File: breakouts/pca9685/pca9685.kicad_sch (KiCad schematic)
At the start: 4 parts, among them J1 Conn_01x03, U1 PCA9685PW

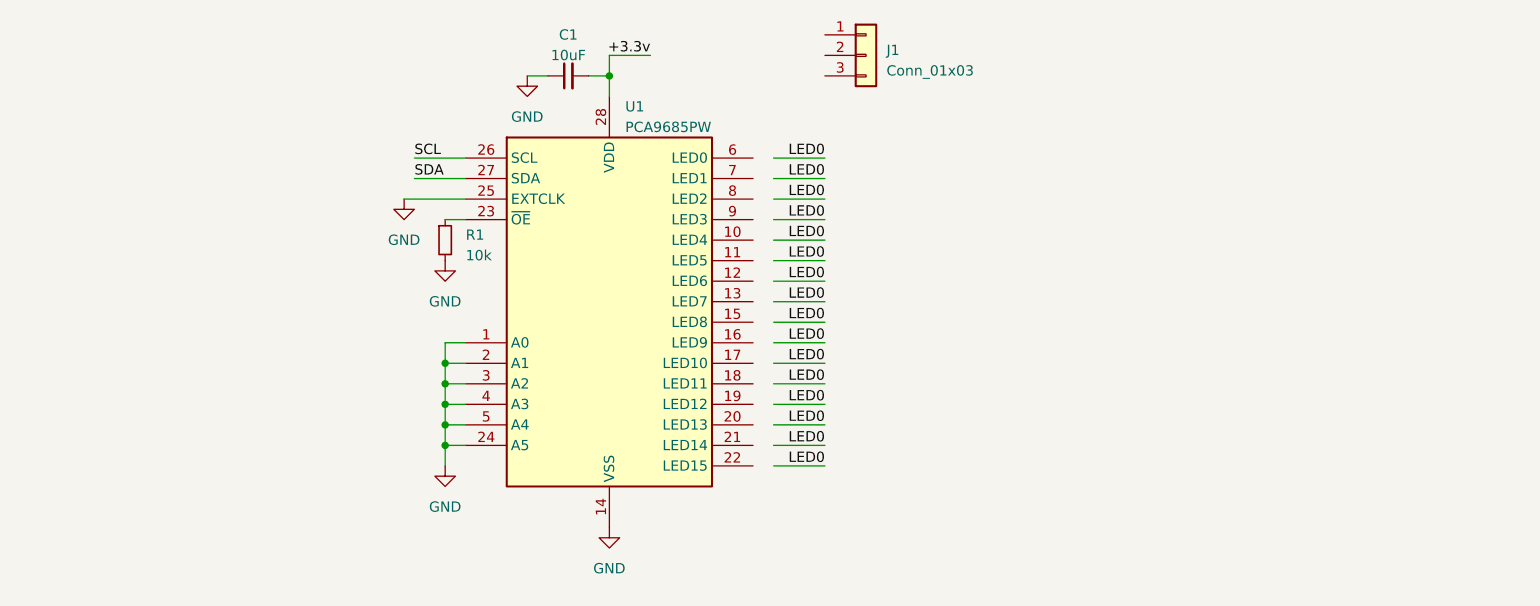
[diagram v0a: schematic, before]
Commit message: Feat[pca9585 breakout]: design complete
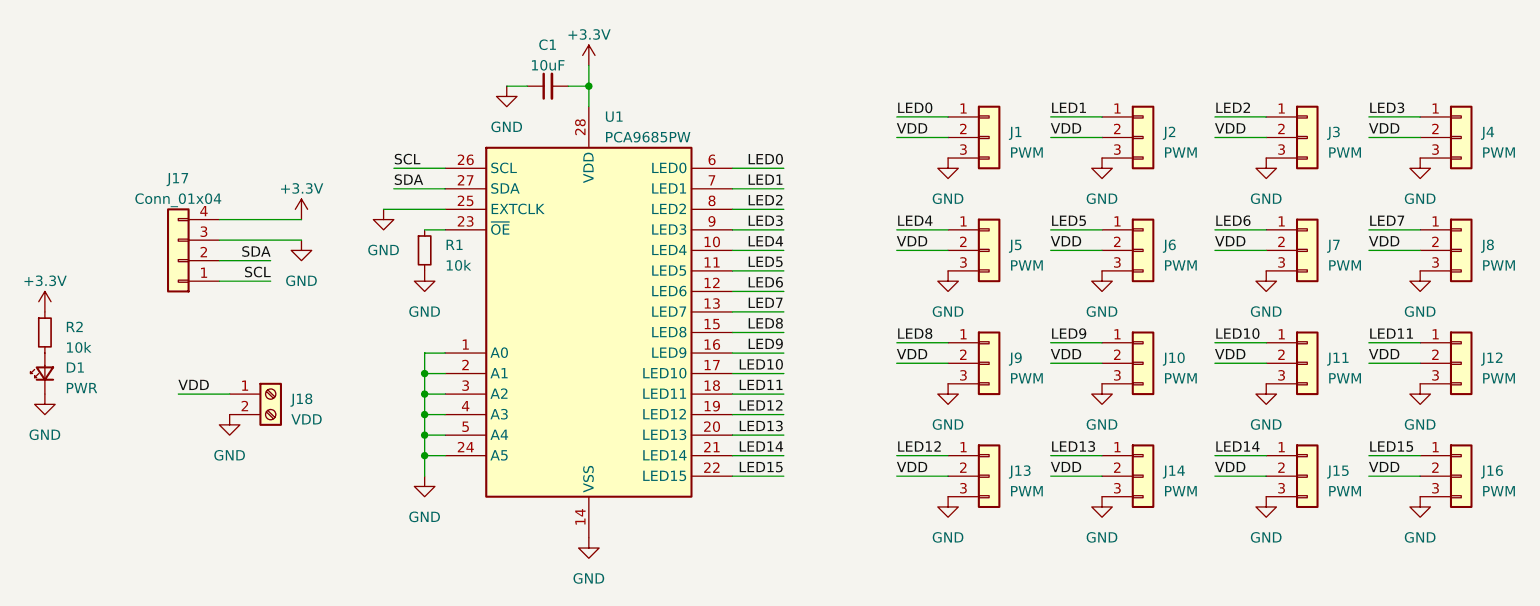
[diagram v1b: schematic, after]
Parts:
- added D1: PWR, LED_SMD:LED_0603_1608Metric, symbol Device:LED_Small
- added J10, J11, J12, J13, J14, J15, J16, J2, J3, J4, J5, J6, J7, J8, J9: PWM, Connector_PinHeader_2.54mm:PinHeader_1x03_P2.54mm_Vertical, symbol Connector_Generic:Conn_01x03
- added J17: Conn_01x04, Connector_PinHeader_2.54mm:PinHeader_1x04_P2.54mm_Vertical, symbol Connector_Generic:Conn_01x04
- added J18: VDD, TerminalBlock:TerminalBlock_Altech_AK300-2_P5.00mm, symbol Connector:Screw_Terminal_01x02
- added R2: 10k, Resistor_SMD:R_0603_1608Metric, symbol Device:R_Small
- J1: value Conn_01x03 -> PWM; footprint (none) -> Connector_PinHeader_2.54mm:PinHeader_1x03_P2.54mm_Vertical
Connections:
- net GND: now also J1.3 (Pin_3), D1.1 (K), J10.3 (Pin_3), J11.3 (Pin_3), J12.3 (Pin_3), J13.3 (Pin_3), J14.3 (Pin_3), J15.3 (Pin_3), J16.3 (Pin_3), J17.3 (Pin_3), J18.2 (Pin_2), J2.3 (Pin_3), J3.3 (Pin_3), J4.3 (Pin_3), J5.3 (Pin_3), J6.3 (Pin_3), J7.3 (Pin_3), J8.3 (Pin_3), J9.3 (Pin_3)
- net LED0: now also J1.1 (Pin_1), U1.6 (LED0)
- net SCL: now also J17.1 (Pin_1)
- net SDA: now also J17.2 (Pin_2)
- net VDD: now reaches J1.2 (Pin_2)
- net VDD: now also J10.2 (Pin_2), J11.2 (Pin_2), J12.2 (Pin_2), J13.2 (Pin_2), J14.2 (Pin_2), J15.2 (Pin_2), J16.2 (Pin_2), J18.1 (Pin_1), J2.2 (Pin_2), J3.2 (Pin_2), J4.2 (Pin_2), J5.2 (Pin_2), J6.2 (Pin_2), J7.2 (Pin_2), J8.2 (Pin_2), J9.2 (Pin_2)
- net LED4: now reaches U1.10 (LED4)
- net LED4: now also J5.1 (Pin_1)
- net LED5: now reaches U1.11 (LED5)
- net LED5: now also J6.1 (Pin_1)
- net LED6: now reaches U1.12 (LED6)
- net LED6: now also J7.1 (Pin_1)
- net LED7: now reaches U1.13 (LED7)
- net LED7: now also J8.1 (Pin_1)
- net LED8: now reaches U1.15 (LED8)
- net LED8: now also J9.1 (Pin_1)
- net LED9: now reaches U1.16 (LED9)
- net LED9: now also J10.1 (Pin_1)
- net LED10: now reaches U1.17 (LED10)
- net LED10: now also J11.1 (Pin_1)
- net LED11: now reaches U1.18 (LED11)
- net LED11: now also J12.1 (Pin_1)
- net LED12: now reaches U1.19 (LED12)
- net LED12: now also J13.1 (Pin_1)
- net LED13: now reaches U1.20 (LED13)
- net LED13: now also J14.1 (Pin_1)
- net LED14: now reaches U1.21 (LED14)
- net LED14: now also J15.1 (Pin_1)
- net LED15: now reaches U1.22 (LED15)
- net LED15: now also J16.1 (Pin_1)
- net LED1: now reaches U1.7 (LED1)
- net LED1: now also J2.1 (Pin_1)
- net LED2: now reaches U1.8 (LED2)
- net LED2: now also J3.1 (Pin_1)
- net LED3: now reaches U1.9 (LED3)
- net LED3: now also J4.1 (Pin_1)
- net +3.3v renamed +3.3V
- net +3.3V: now also J17.4 (Pin_4), R2.1
- new net: D1.2 (A), R2.2
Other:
- company: (none) -> MUREX Robotics [Byran Huang]
- title: (none) -> PCA9685 Breakout
- moved on the sheet: C1, J1, R1, U1
